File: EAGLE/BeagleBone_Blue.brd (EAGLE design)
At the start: 86.4 x 54.6 mm, 306 parts, among them J2 SERVO_HEADERS_8X, M1 JST_ZH_2, M2 JST_ZH_2, M3 JST_ZH_2, M4 JST_ZH_2, Q1 MOSFET-N, T1 BSS138W-7-F, T2 BSS138W-7-F, U1 TCAN1051HV, U10 TXS0108ERGYR, U13 EMMC, U2 SN74LV1T126DBVR, U3 TPD4S012DRY, U4 TPD4S012DRY, U5 24LC_32AT-I/OT, U6 SN74LVC1G07_DCK_5, U7 WL1835MODGBMOCT, U9 TXS0108ERGYR, X2 SCHA5B0200, X3 USB1, X4 10118192-0001LF, Y1 24 MHz, Y2 32.768kHz

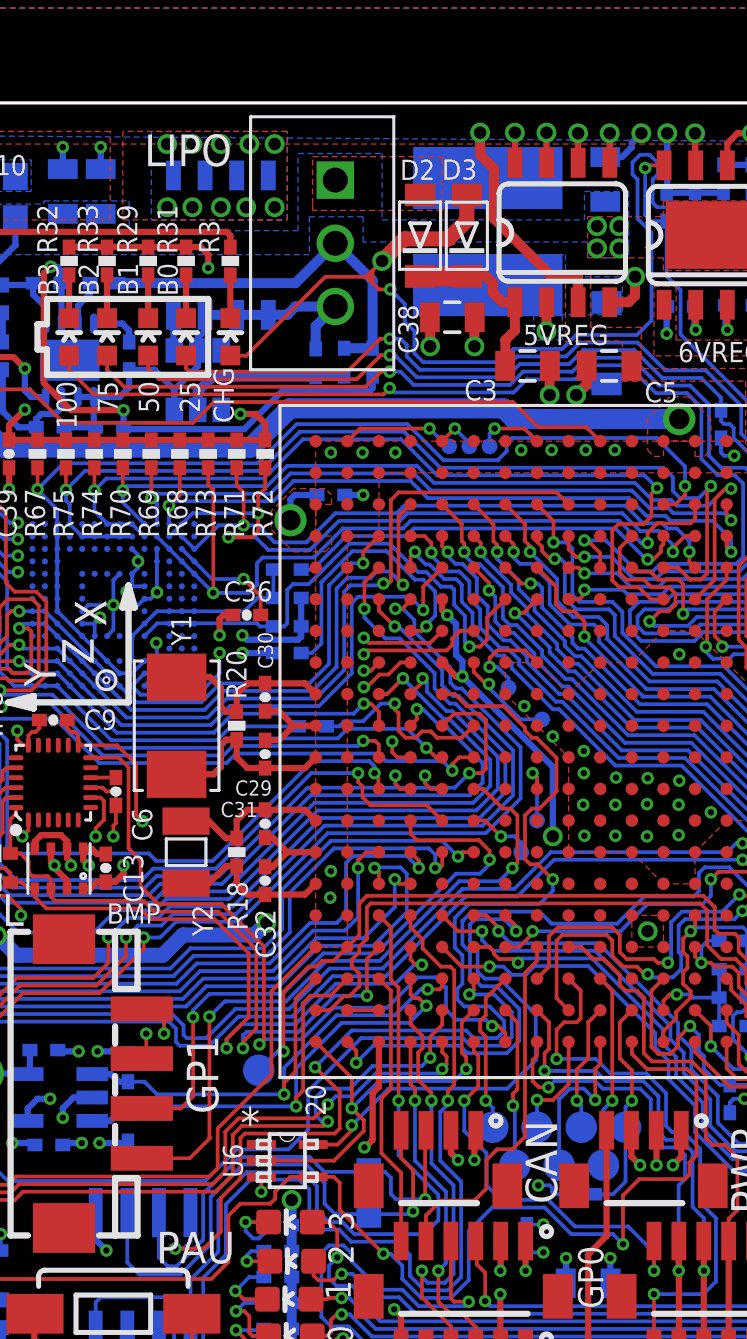
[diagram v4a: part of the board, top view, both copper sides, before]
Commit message: Fixing silkscreen issues.
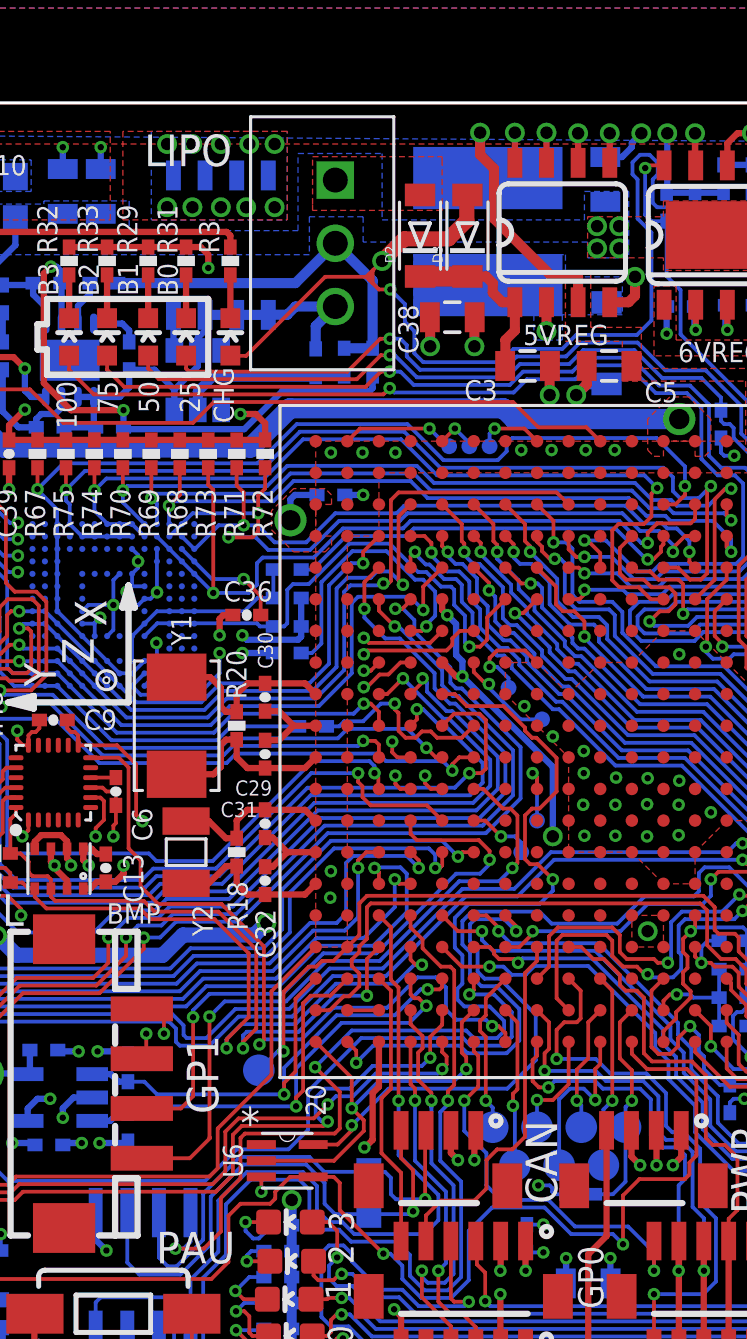
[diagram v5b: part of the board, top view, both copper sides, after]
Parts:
- D2, D3: device adafruit:SOD-123FL -> BeagleBone_Blue:ADAFRUIT_SOD-123FL
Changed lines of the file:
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@@
 <attribute name="VALUE" x="39.751" y="-43.8785" size="0.8128" layer="27" rot="R180"/>
-</element>
-<element name="D2" library="adafruit" package="SOD-123FL" value="" x="43.942" y="-5.334" smashed="yes" rot="R90">
-<attribute name="NAME" x="44.5467" y="-2.2827" size="0.8128" layer="25" rot="R180"/>
-<attribute name="VALUE" x="45.226" y="-6.434" size="0.4064" layer="27" rot="R90"/>
-</element>
-<element name="D3" library="adafruit" package="SOD-123FL" value="" x="45.8216" y="-5.334" smashed="yes" rot="R90">
-<attribute name="NAME" x="46.2358" y="-2.27" size="0.8128" layer="25" rot="R180"/>
-<attribute name="VALUE" x="47.1056" y="-6.434" size="0.4064" layer="27" rot="R90"/>
 </element>
 <element name="B0" library="SparkFun-LED" package="LED-0603" value="RED" x="34.544" y="-9.398" smashed="yes">
@@
 </element>
 <element name="D1" library="BeagleBone_Blue" package="ADAFRUIT_SOD-123FL" value="" x="51.435" y="-9.652" rot="MR270"/>
+<element name="D2" library="BeagleBone_Blue" package="ADAFRUIT_SOD-123FL" value="" x="43.942" y="-5.334" rot="R90"/>
+<element name="D3" library="BeagleBone_Blue" package="ADAFRUIT_SOD-123FL" value="" x="45.847" y="-5.334" rot="R90"/>
 </elements>
 <signals>
@@
 <contactref element="H2" pad="24"/>
 <contactref element="C11" pad="+"/>
-<contactref element="D2" pad="A"/>
 <contactref element="CHGIC" pad="9"/>
 <contactref element="C26" pad="1"/>
@@
 <via x="77.089" y="-26.416" extent="1-16" drill="0.5"/>
 <wire x1="68.5038" y1="-44.831" x2="70.6374" y2="-44.831" width="0.1524" layer="16"/>
+<contactref element="D2" pad="A"/>
 </signal>
 <signal name="N$79">
-<contactref element="D3" pad="C"/>
-<contactref element="D2" pad="C"/>
 <contactref element="C3" pad="1"/>
 <contactref element="5VREG" pad="1"/>
-<wire x1="43.942" y1="-6.9715" x2="45.8216" y2="-6.9715" width="0.8128" layer="1"/>
 <wire x1="47.36" y1="-10.5664" x2="47.36" y2="-10.2218" width="0.4064" layer="1"/>
 <wire x1="47.36" y1="-10.2218" x2="47.371" y2="-10.2108" width="0.4064" layer="1"/>
@@
 <wire x1="47.371" y1="-9.525" x2="47.752" y2="-9.144" width="0.4064" layer="1"/>
 <wire x1="47.752" y1="-9.144" x2="47.752" y2="-8.007" width="0.4064" layer="1"/>
-<wire x1="45.8216" y1="-6.9715" x2="46.5955" y2="-6.9715" width="0.4064" layer="1"/>
 <wire x1="46.5955" y1="-6.9715" x2="46.863" y2="-7.239" width="0.4064" layer="1"/>
 <wire x1="46.863" y1="-7.239" x2="46.863" y2="-7.62" width="0.4064" layer="1"/>
 <wire x1="46.863" y1="-7.62" x2="47.25" y2="-8.007" width="0.4064" layer="1"/>
 <wire x1="47.25" y1="-8.007" x2="47.752" y2="-8.007" width="0.4064" layer="1"/>
+<contactref element="D2" pad="C"/>
+<contactref element="D3" pad="C"/>
+<wire x1="43.942" y1="-6.9715" x2="45.847" y2="-6.9715" width="0.8128" layer="1"/>
+<wire x1="46.5955" y1="-6.9715" x2="45.847" y2="-6.9715" width="0.4064" layer="1"/>
 </signal>
 <signal name="N$17">
@@
 <contactref element="C7" pad="1"/>
 <contactref element="C12" pad="1"/>
-<contactref element="D3" pad="A"/>
 <contactref element="R1" pad="1"/>
 <polygon width="0.254" layer="1">
@@
 <wire x1="40.132" y1="-6.985" x2="41.783" y2="-6.985" width="0.1524" layer="1"/>
 <wire x1="45.085" y1="-5.461" x2="45.8216" y2="-4.7244" width="0.6096" layer="1"/>
-<wire x1="45.8216" y1="-4.7244" x2="45.8216" y2="-3.6965" width="0.6096" layer="1"/>
 <wire x1="41.8338" y1="-6.9342" x2="39.4208" y2="-6.9342" width="0.6096" layer="2"/>
 <wire x1="39.4208" y1="-6.9342" x2="38.862" y2="-7.493" width="0.6096" layer="2"/>
@@
 <wire x1="42.037" y1="-7.239" x2="41.91" y2="-7.112" width="0.1524" layer="1"/>
 <wire x1="41.91" y1="-7.112" x2="41.91" y2="-6.858" width="0.1524" layer="1"/>
+<contactref element="D3" pad="A"/>
+<wire x1="45.847" y1="-3.6965" x2="45.8216" y2="-3.6965" width="0.6096" layer="1"/>
+<wire x1="45.8216" y1="-3.6965" x2="45.8216" y2="-4.7244" width="0.6096" layer="1"/>
 </signal>
 <signal name="UART4_RX">

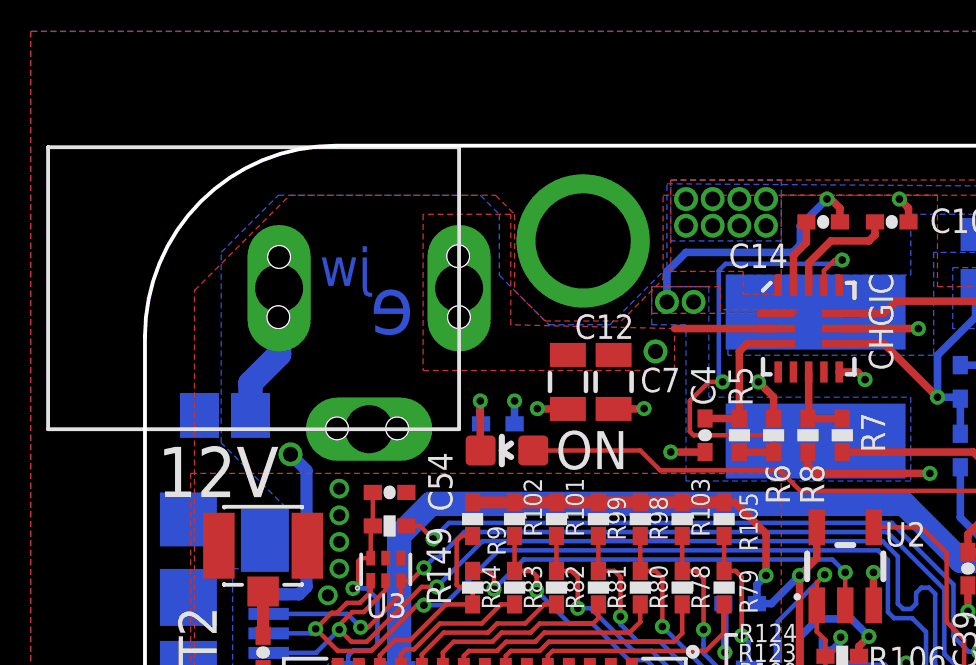
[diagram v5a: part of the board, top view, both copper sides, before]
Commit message: Moved R24 and R107 for manufacturing concerns.  Cleaned up some power pours on the top and bottom.
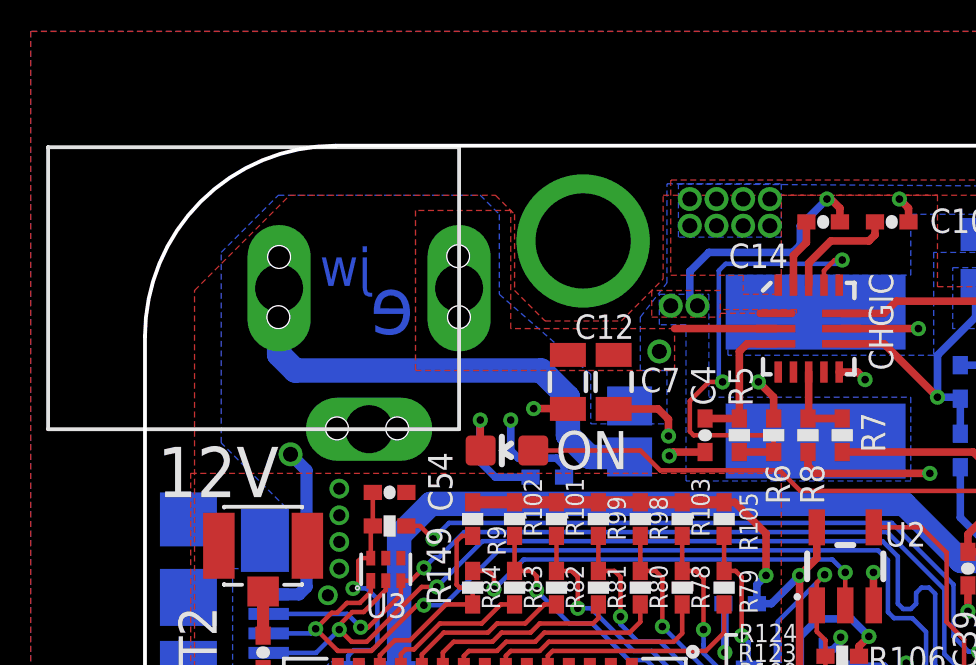
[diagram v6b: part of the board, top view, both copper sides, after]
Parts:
- moved R107 13.5 mm to (16.2, -9.53), turned to 90 degrees
- moved R24 2.43 mm to (13.4, -11.0)
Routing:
- net GND: track 227.9 -> 243.7 mm
- net PWR_LED: track 2.44 -> 4.43 mm
- net N$55: track 8.74 -> 8.21 mm

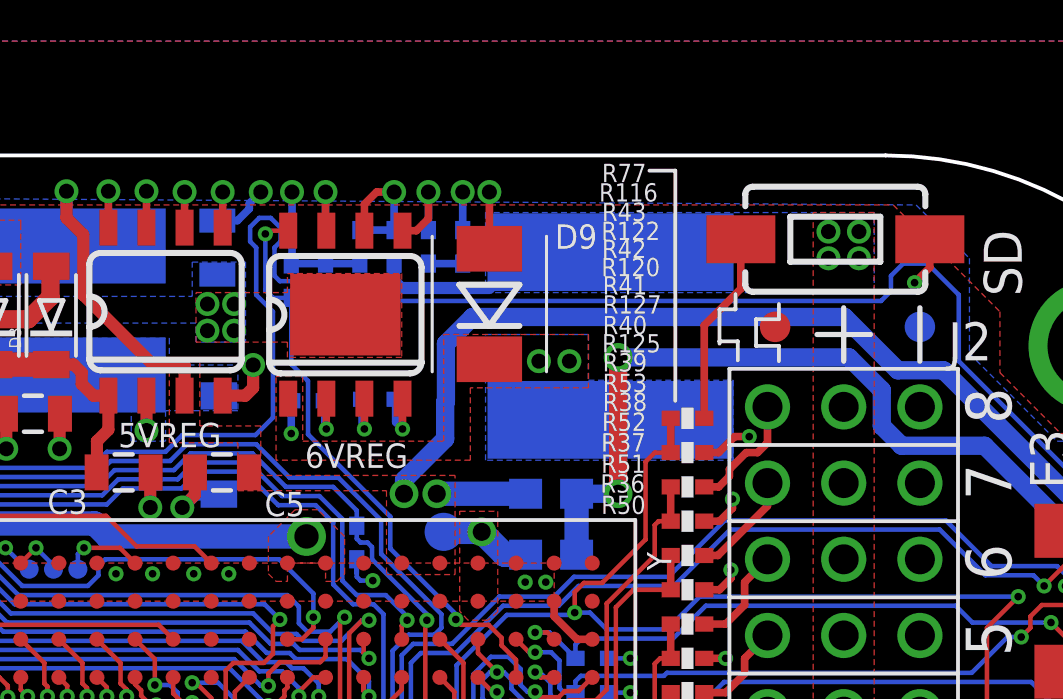
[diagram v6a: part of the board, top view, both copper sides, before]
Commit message: Moved L3 for manufacturing issues.
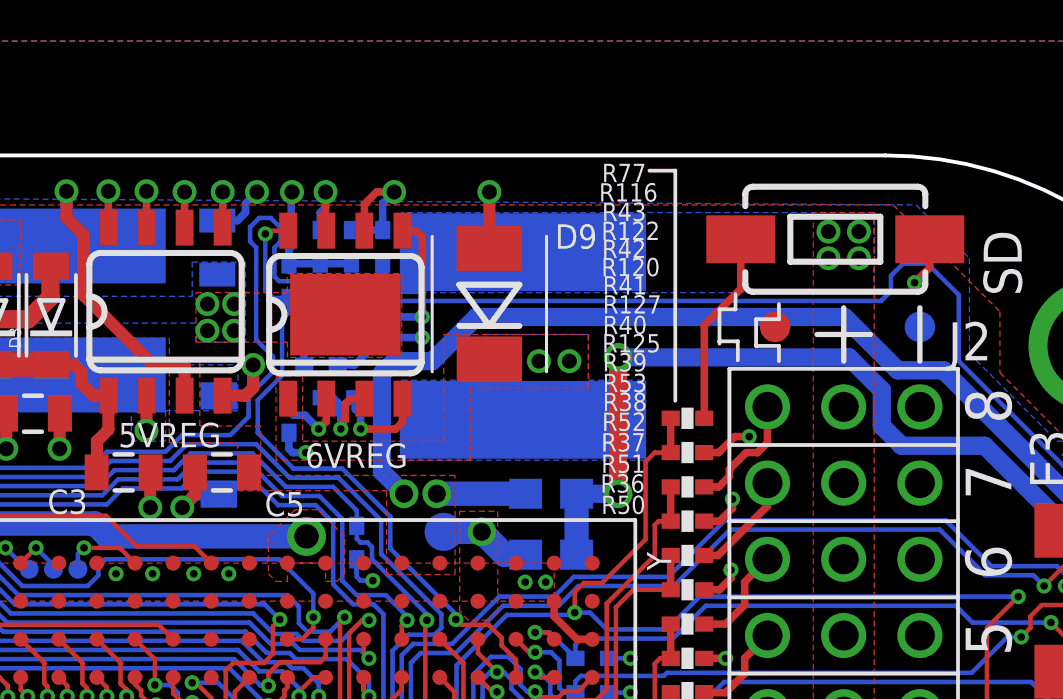
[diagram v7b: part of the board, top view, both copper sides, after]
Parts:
- moved C24 6.15 mm to (54.8, -6.99), turned to 0 degrees
- moved R45 4.57 mm to (54.8, -5.89), turned to 180 degrees
- moved L3 2.92 mm to (61.6, -6.02)
- moved R47 1.35 mm to (55.4, -8.08)
- moved C22 0.81 mm to (53.8, -8.69), turned to 270 degrees
- moved R49 0.38 mm to (56.9, -3.05)
- moved R48 0.28 mm to (55.9, -3.05)
- moved C21 0.18 mm to (54.8, -3.05)
- moved R46 0.08 mm to (53.8, -4.19)
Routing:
- net N$63: track 3.19 -> 6.45 mm
- net GND: track 243.7 -> 246.5 mm
- net N$62: track 9.33 -> 7.30 mm
- net SERVO_EN: track 19.9 -> 21.7 mm
- net N$61: track 2.10 -> 3.39 mm
- net 5.0V: track 144.3 -> 145.6 mm
- net N$53: track 1.97 -> 2.74 mm

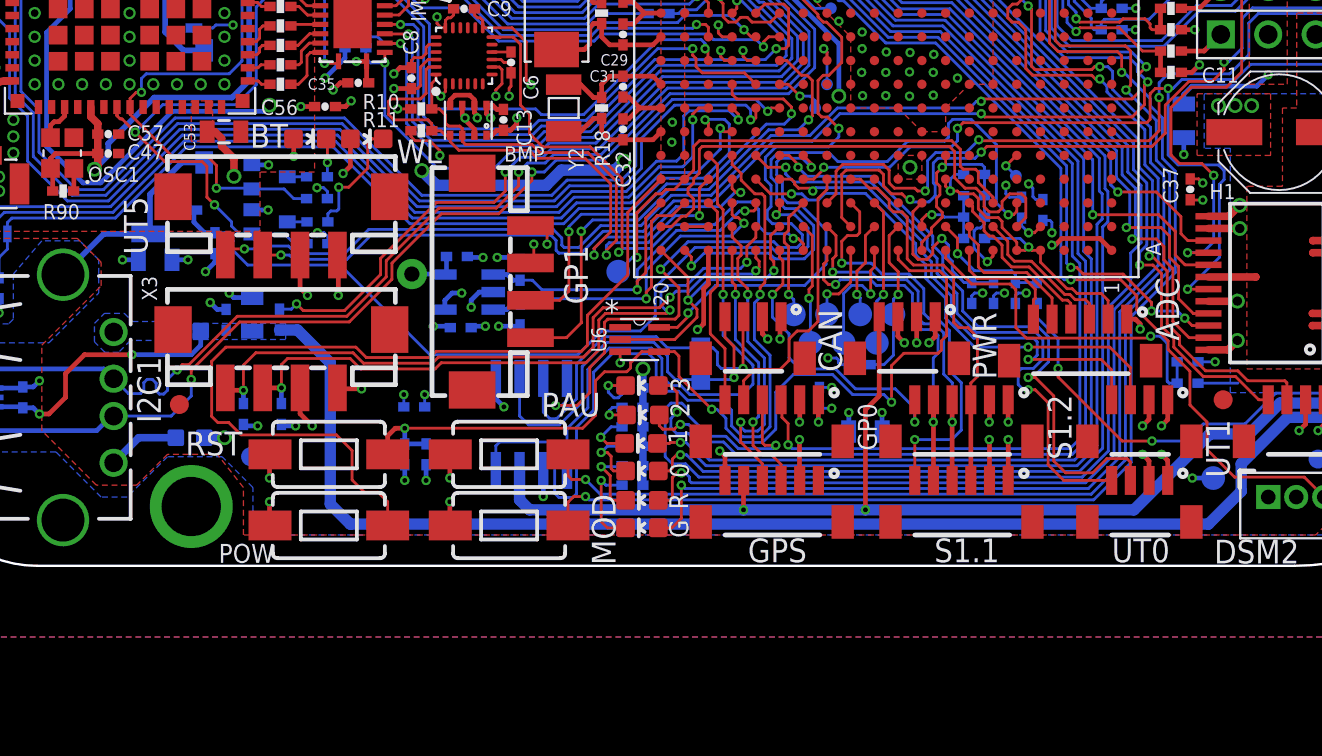
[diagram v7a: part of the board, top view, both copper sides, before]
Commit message: Schematic updates for Rev A2.  See Issues.
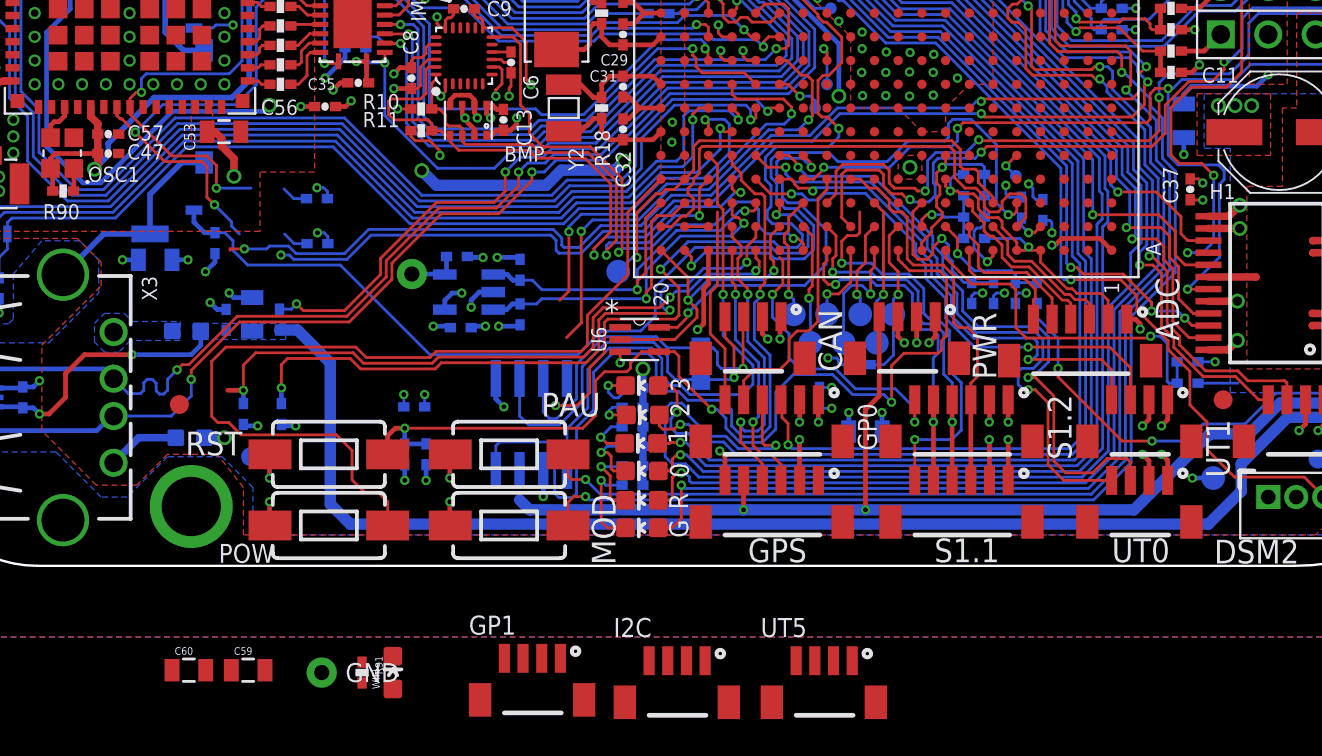
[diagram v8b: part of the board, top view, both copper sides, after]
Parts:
- removed BT, WL: BLUE, BeagleBone_Blue:BEAGLEBONE_BLUE_LED-0603
- removed I2C1: H4P-SMD-2.0, Seeed-Connector -2016:HW4-SMD-2.0
- removed R95: 1K, Strawson_Eagle_Lib:0402-RES
- removed T1, T2: BSS138W-7-F, GHI Transistors:SOT-323(DIODES)
- added C59, C60: 10uF, SparkFun-Capacitors:0805
- added GND: TESTPAD/W_HOLE_1X1, GHI2:TESTPAD/W_HOLE_1X1
- added I2C: JST_SH_4, Strawson_Eagle_Lib:JST_SH_4_SMD
- added WIFI: GREEN, BeagleBone_Blue:BEAGLEBONE_BLUE_LED-0603
- GP1, UT5: value H4P-SMD-2.0 -> JST_SH_4; device Seeed-Connector -2016:HW4-SMD-2.0 -> Strawson_Eagle_Lib:JST_SH_4_SMD
- R91: value 1K -> 240
- moved UT5 37.9 mm to (49.5, -61.0)
- moved R91 24.2 mm to (23.7, -60.3), flipped to the top, turned to 270 degrees
- moved GP1 21.5 mm to (33.9, -60.8), turned to 0 degrees
- renumbered TP10 to WP
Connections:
- removed net N$44: R91.2, WL.C
- removed net N$46: BT.C, R95.2
- removed net N$64: R91.1, T1.D
- removed net N$68: R95.1, T2.D
- new net N$20: R91.1, WIFI.C
- new net WIFI_LED: SIP.A15, WIFI.A
- net 3.3V: now also C59.1, GP1.2, I2C.2, UT5.2; no longer BT.A, GP1.3, I2C1.3, UT5.3, WL.A
- net 5.0V: no longer U1.3
- net BT_EN_1V8: no longer T2.G
- net GND: now also C59.2, C60.1, GND.P$1, GP1.1, I2C.1, R91.2, UT5.1; no longer GP1.4, I2C1.4, T1.S, T2.S, UT5.4
- net GPIO_0_3: now also SIP.C12; no longer SIP.C18
- net GPIO_1_0: now also GP1.3; no longer GP1.1
- net GPIO_1_1: now also GP1.4; no longer GP1.2
- net I2C1_SCL: now also I2C.3; no longer I2C1.1
- net I2C1_SDA: now also I2C.4; no longer I2C1.2
- net MDIR_2B: now also R140.1, SIP.V4; no longer R131.2, SIP.U2
- net SPI1_SS1: now also SIP.H18; no longer SIP.C12
- net SPI1_SS2: now also SIP.C18; no longer SIP.A15
- net SYS_5V: now also U1.3
- net UART5_RX: now also R131.2, SIP.U2, UT5.3; no longer R140.1, SIP.V4, UT5.1
- net UART5_TX: now also UT5.4; no longer UT5.2
- net VDD_1V8: now also C60.2
- net WL_EN_1V8: no longer T1.G
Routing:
- net UART5_RX: track 91.8 -> 39.3 mm
- net MDIR_2B: track 40.4 -> 91.5 mm
- net 3.3V: track 148.4 -> 139.8 mm, vias 66 -> 61
- net GND: track 246.5 -> 239.4 mm, vias 223 -> 218
- net N$44: track 6.53 -> 0.00 mm, vias 1 -> 0
- net WL_EN_1V8: track 34.3 -> 31.9 mm
- net N$46: track 2.06 -> 0.00 mm, vias 1 -> 0
- net GPIO_1_0: track 27.0 -> 25.1 mm
- net BT_EN_1V8: track 30.5 -> 28.7 mm
- net 5.0V: track 145.6 -> 144.0 mm
- net GPIO_1_1: track 24.6 -> 23.0 mm
- net N$64: track 1.06 -> 0.00 mm
- net N$68: track 1.03 -> 0.00 mm
- net I2C1_SDA: track 35.2 -> 34.2 mm
- net UART5_TX: track 91.8 -> 90.8 mm
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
